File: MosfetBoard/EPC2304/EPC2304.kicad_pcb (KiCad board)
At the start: 4 copper layers, 120 x 75 mm, 176 parts, among them J10 DriverConn, J14 BATT-Conn2, J4 PhaseConn, J5 PhaseConn, J6 PhaseConn, J7 DriverConn, J8 DriverConn, J9 BATT-Conn1, Q1 EPC2304, Q13 EPC2304, Q14 EPC2304, Q15 EPC2304, Q2 EPC2304, Q3 EPC2304, Q4 EPC2304, Q5 EPC2304, Q6 EPC2304, Q7 EPC2304, Q8 EPC2304, Q9 EPC2304, U1 2EDF7275KXUMA1, U2 2EDF7275KXUMA1, U3 2EDF7275KXUMA1, U4 MT9223CT-50BR5, U5 MT9223CT-50BR5, U6 MT9223CT-50BR5

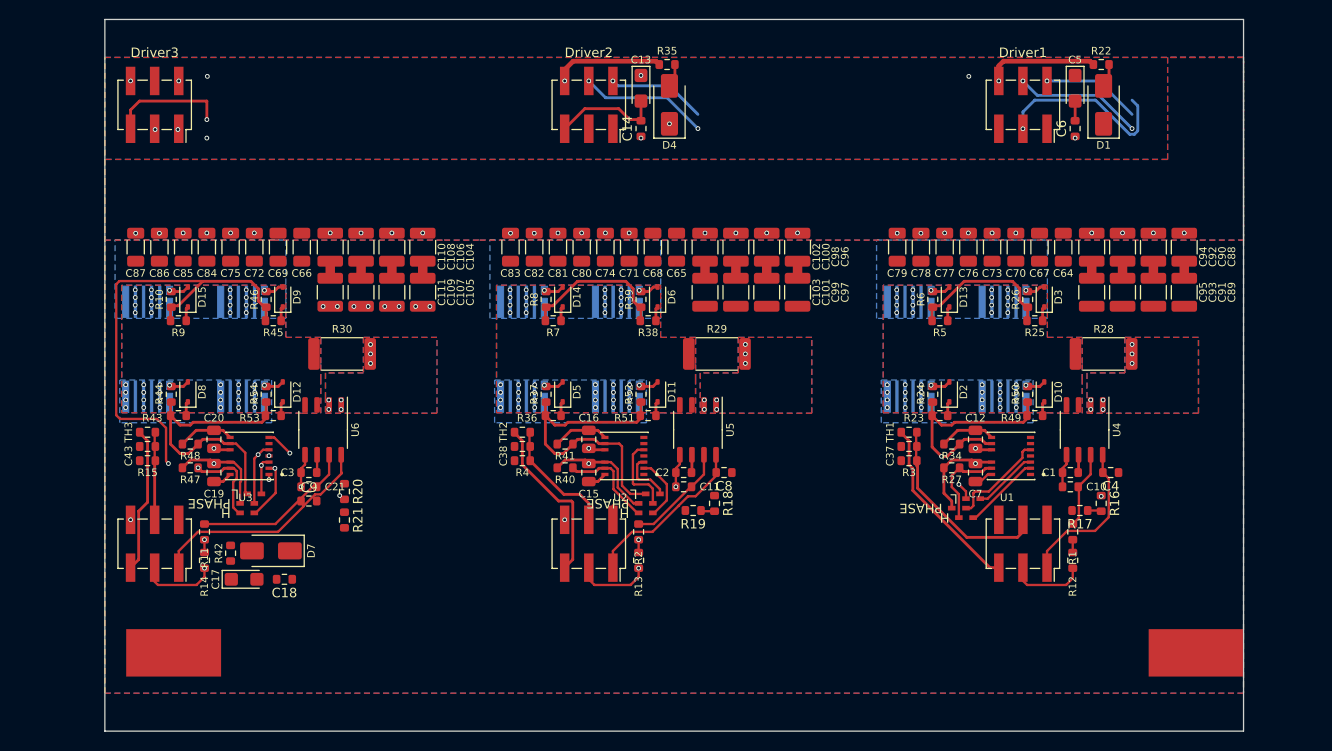
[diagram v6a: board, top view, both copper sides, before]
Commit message: v2.10.0 - Low side shunt and hall sensor - epc routed
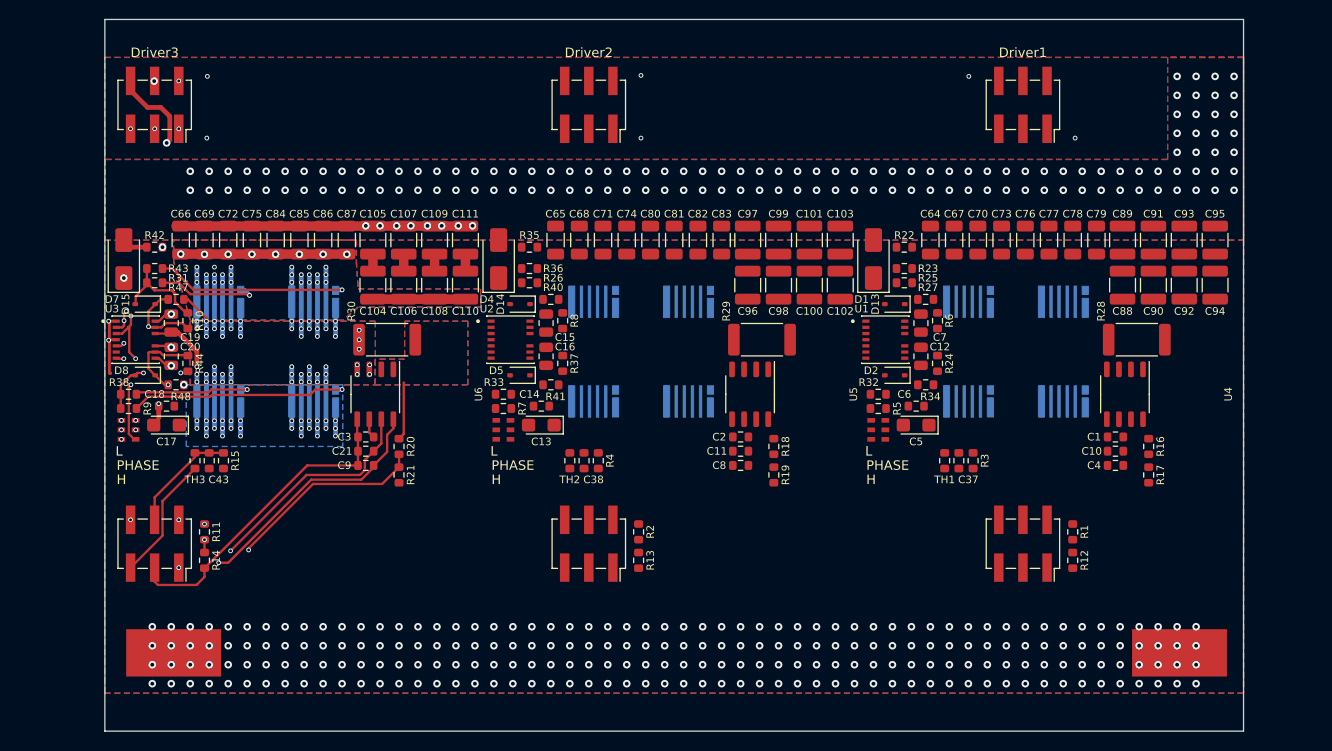
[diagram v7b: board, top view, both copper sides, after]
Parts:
- removed D10, D11, D12, D3, D6, D9: 1N5819WS, Diode_SMD:D_SOD-323
- removed R39, R46, R50, R52, R54: 10, Resistor_SMD:R_0603_1608Metric
- removed R45, R49, R51, R53: 1, Resistor_SMD:R_0603_1608Metric
- added R31: 2.2, Resistor_SMD:R_0603_1608Metric, F.Cu at (110.2, 81.8)
- added R32: 2.2, Resistor_SMD:R_0603_1608Metric, F.Cu at (186.5, 93.5)
- added R33: 2.2, Resistor_SMD:R_0603_1608Metric, F.Cu at (147.0, 93.5)
- R10, R24, R37, R44, R6, R8: value 10 -> 3.3
- R23, R25, R36, R38, R43, R5, R7, R9: value 1 -> 2.2
- R26: value 10 -> 2.2
- moved R38 55.3 mm to (107.5, 93.5)
- moved R26 52.5 mm to (149.8, 81.8), turned to 0 degrees
- moved C5 39.3 mm to (190.5, 96.8), turned to 180 degrees
- moved C13 37.0 mm to (151.0, 96.8), turned to 180 degrees
- moved D7 34.4 mm to (107.0, 79.2), turned to 90 degrees
- moved C6 33.7 mm to (190.5, 94.8), turned to 180 degrees
- moved R42 33.2 mm to (110.2, 78.0), turned to 180 degrees
- moved C14 31.1 mm to (151.0, 94.8), turned to 180 degrees
- moved D1 29.2 mm to (186.0, 79.2)
- moved R22 28.3 mm to (189.2, 78.0), turned to 180 degrees
- moved D4 24.2 mm to (146.5, 79.2)
- moved R35 24.1 mm to (149.8, 78.0), turned to 180 degrees
- moved C83 22.3 mm to (170.0, 77.2), turned to 90 degrees
- moved C87 22.3 mm to (130.5, 77.2), turned to 90 degrees
- moved C18 22.1 mm to (111.5, 94.8)
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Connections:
- D13 pad 1: Net-(D13-K) -> /PhaseMosfets1/PH
- D13 pad 2: Net-(D13-A) -> /PhaseMosfets1/HIGH
- D14 pad 1: Net-(D14-K) -> /PhaseMosfets2/PH
- D14 pad 2: Net-(D14-A) -> /PhaseMosfets2/HIGH
- D15 pad 1: Net-(D15-K) -> /PhaseMosfets3/PH
- D15 pad 2: Net-(D15-A) -> /PhaseMosfets3/HIGH
- D2 pad 1: Net-(D2-K) -> /PhaseMosfets1/PL
- D2 pad 2: Net-(D2-A) -> /PhaseMosfets1/LOW
- D5 pad 1: Net-(D5-K) -> /PhaseMosfets2/PL
- D5 pad 2: Net-(D5-A) -> /PhaseMosfets2/LOW
- D8 pad 1: Net-(D8-K) -> /PhaseMosfets3/PL
- D8 pad 2: Net-(D8-A) -> /PhaseMosfets3/LOW
- Q1 pad 1: Net-(D13-A) -> Net-(Q1-G)
- Q13 pad 1: Net-(D3-A) -> Net-(Q13-G)
- Q14 pad 1: Net-(D6-A) -> Net-(Q14-G)
- Q15 pad 1: Net-(D9-A) -> Net-(Q15-G)
- Q2 pad 1: Net-(D14-A) -> Net-(Q2-G)
- Q3 pad 1: Net-(D15-A) -> Net-(Q3-G)
- Q4 pad 1: Net-(D2-A) -> Net-(Q4-G)
- Q5 pad 1: Net-(D5-A) -> Net-(Q5-G)
- Q6 pad 1: Net-(D8-A) -> Net-(Q6-G)
- Q7 pad 1: Net-(D10-A) -> Net-(Q7-G)
- Q8 pad 1: Net-(D11-A) -> Net-(Q8-G)
- Q9 pad 1: Net-(D12-A) -> Net-(Q9-G)
- R10 pad 2: Net-(D15-A) -> /PhaseMosfets3/HIGH
- R23 pad 1: /PhaseMosfets1/PL -> /PhaseMosfets1/HIGH
- R23 pad 2: Net-(D2-K) -> Net-(Q13-G)
- R24 pad 2: Net-(D2-A) -> /PhaseMosfets1/LOW
- R25 pad 1: /PhaseMosfets1/PH -> /PhaseMosfets1/HIGH
- R25 pad 2: Net-(D3-K) -> Net-(Q1-G)
- R26 pad 1: /PhaseMosfets1/PH -> /PhaseMosfets2/HIGH
- R26 pad 2: Net-(D3-A) -> Net-(Q2-G)
- R36 pad 1: /PhaseMosfets2/PL -> /PhaseMosfets2/HIGH
- R36 pad 2: Net-(D5-K) -> Net-(Q14-G)
- R37 pad 2: Net-(D5-A) -> /PhaseMosfets2/LOW
- R38 pad 1: /PhaseMosfets2/PH -> /PhaseMosfets3/LOW
- R38 pad 2: Net-(D6-K) -> Net-(Q6-G)
- R43 pad 1: /PhaseMosfets3/PL -> /PhaseMosfets3/HIGH
- R43 pad 2: Net-(D8-K) -> Net-(Q15-G)
- R44 pad 2: Net-(D8-A) -> /PhaseMosfets3/LOW
- R5 pad 1: /PhaseMosfets1/PH -> /PhaseMosfets1/LOW
- R5 pad 2: Net-(D13-K) -> Net-(Q7-G)
- R6 pad 2: Net-(D13-A) -> /PhaseMosfets1/HIGH
- R7 pad 1: /PhaseMosfets2/PH -> /PhaseMosfets2/LOW
- R7 pad 2: Net-(D14-K) -> Net-(Q8-G)
- R8 pad 2: Net-(D14-A) -> /PhaseMosfets2/HIGH
- R9 pad 1: /PhaseMosfets3/PH -> /PhaseMosfets3/LOW
- R9 pad 2: Net-(D15-K) -> Net-(Q9-G)
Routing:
- net /PhaseMosfets3/PHASE: track 16.9 -> 149.1 mm, vias 41 -> 64
- net +BATT: track 0.00 -> 101.2 mm, vias 30 -> 170
- net -BATT: track 45.5 -> 135.6 mm, vias 20 -> 269
- net /PhaseMosfets1/DRV_POWER: track 66.8 -> 0.00 mm, vias 2 -> 0
- net /PhaseMosfets2/DRV_POWER: track 64.3 -> 0.00 mm, vias 2 -> 0
- net /PhaseMosfets3/3.3V_IN: track 86.1 -> 38.3 mm, vias 2 -> 3
- net /PhaseMosfets3/L: track 82.2 -> 34.6 mm, vias 2 -> 4
- net /PhaseMosfets3/LOCKOUT: track 81.3 -> 36.5 mm, vias 2 -> 3
- net /PhaseMosfets3/H: track 86.1 -> 43.1 mm, vias 2 -> 4
- net /PhaseMosfets3/PH: track 61.2 -> 22.0 mm
- net /PhaseMosfets2/PL: track 33.3 -> 0.00 mm
- net /PhaseMosfets1/PL: track 30.4 -> 0.00 mm, vias 2 -> 0
- net /PhaseMosfets3/V_SENSE: track 0.00 -> 29.8 mm, vias 1 -> 2
- net /PhaseMosfets1/L: track 26.4 -> 0.00 mm, vias 1 -> 0
- net /PhaseMosfets2/PH: track 26.0 -> 0.00 mm
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- removed copper zone on B.Cu, net /PhaseMosfets1/PHASE
- removed copper zone on F.Cu, net /PhaseMosfets1/PHASE
- removed copper zone on In1.Cu, net /PhaseMosfets1/PHASE
- removed copper zone on In2.Cu, net /PhaseMosfets1/PHASE
- removed copper zone on B.Cu, net /PhaseMosfets1/PHASE_OUT
- removed copper zone on F.Cu, net /PhaseMosfets1/PHASE_OUT
- removed copper zone on In1.Cu, net /PhaseMosfets1/PHASE_OUT
- removed copper zone on In2.Cu, net /PhaseMosfets1/PHASE_OUT
- removed copper zone on B.Cu, net /PhaseMosfets2/PHASE
- removed copper zone on F.Cu, net /PhaseMosfets2/PHASE
- removed copper zone on In1.Cu, net /PhaseMosfets2/PHASE
- removed copper zone on In2.Cu, net /PhaseMosfets2/PHASE
- removed copper zone on B.Cu, net /PhaseMosfets2/PHASE_OUT
- removed copper zone on F.Cu, net /PhaseMosfets2/PHASE_OUT
- removed copper zone on In1.Cu, net /PhaseMosfets2/PHASE_OUT
- removed copper zone on In2.Cu, net /PhaseMosfets2/PHASE_OUT
- removed copper zone on In2.Cu, net /PhaseMosfets3/PHASE

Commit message: v2.10.0 - Low side shunt and hall sensor - epc finished
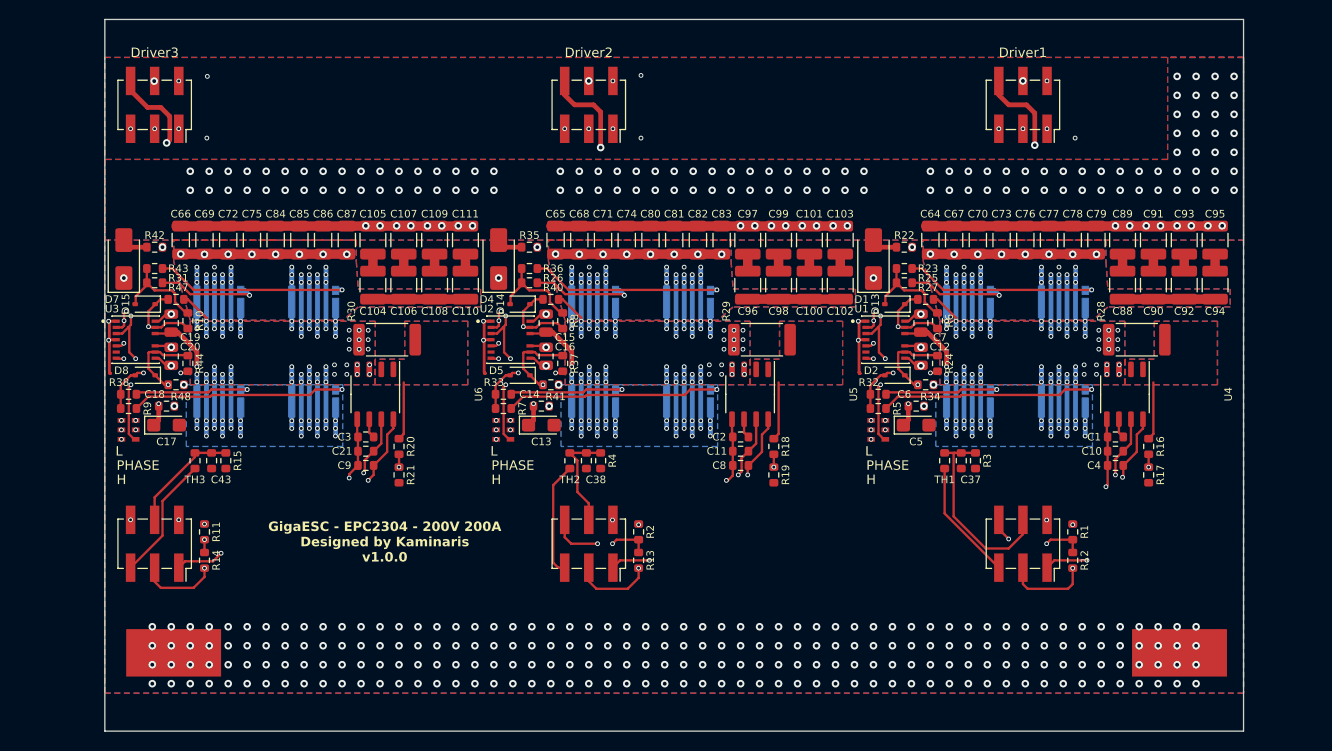
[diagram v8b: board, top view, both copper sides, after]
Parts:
- R10, R24, R37, R44, R6, R8: value 3.3 -> 4.7
- moved C37 0.25 mm to (195.2, 100.5)
- moved C38 0.25 mm to (155.8, 100.5)
- moved C43 0.25 mm to (116.2, 100.5)
- moved R15 0.25 mm to (117.8, 100.5)
- moved R3 0.25 mm to (196.8, 100.5)
- moved R4 0.25 mm to (157.2, 100.5)
- turned C13 to 0 degrees
- turned C17 to 0 degrees
- turned C5 to 0 degrees
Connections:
- C13 pad 1: -BATT -> /PhaseMosfets2/3.3V_IN
- C13 pad 2: /PhaseMosfets2/3.3V_IN -> -BATT
- C17 pad 1: -BATT -> /PhaseMosfets3/3.3V_IN
- C17 pad 2: /PhaseMosfets3/3.3V_IN -> -BATT
- C5 pad 1: -BATT -> /PhaseMosfets1/3.3V_IN
- C5 pad 2: /PhaseMosfets1/3.3V_IN -> -BATT
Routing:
- net -BATT: track 135.6 -> 416.3 mm, vias 269 -> 349
- net +BATT: track 101.2 -> 303.7 mm, vias 170 -> 236
- net /PhaseMosfets2/PHASE: track 0.00 -> 149.1 mm, vias 0 -> 74
- net /PhaseMosfets1/PHASE: track 0.00 -> 149.1 mm, vias 0 -> 74
- net /PhaseMosfets1/H: track 0.00 -> 53.0 mm, vias 0 -> 4
- net /PhaseMosfets1/3.3V_IN: track 0.00 -> 47.8 mm, vias 0 -> 3
- net /PhaseMosfets1/LOCKOUT: track 0.00 -> 47.3 mm, vias 0 -> 3
- net /PhaseMosfets2/H: track 0.00 -> 47.0 mm, vias 0 -> 4
- net /PhaseMosfets1/L: track 0.00 -> 44.7 mm, vias 0 -> 4
- net /PhaseMosfets1/DRV_POWER: track 0.00 -> 44.1 mm, vias 0 -> 3
- net /PhaseMosfets2/3.3V_IN: track 0.00 -> 41.5 mm, vias 0 -> 3
- net /PhaseMosfets2/LOCKOUT: track 0.00 -> 41.0 mm, vias 0 -> 3
- net /PhaseMosfets2/L: track 0.00 -> 38.4 mm, vias 0 -> 4
- net /PhaseMosfets2/DRV_POWER: track 0.00 -> 38.0 mm, vias 0 -> 3
- net /PhaseMosfets2/SH-: track 0.00 -> 31.8 mm, vias 0 -> 2
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- added copper zone on B.Cu, net /PhaseMosfets1/PHASE
- added copper zone on F.Cu, net /PhaseMosfets1/PHASE
- added copper zone on In1.Cu, net /PhaseMosfets1/PHASE
- added copper zone on B.Cu, net /PhaseMosfets1/PHASE_OUT
- added copper zone on F.Cu, net /PhaseMosfets1/PHASE_OUT
- added copper zone on In1.Cu, net /PhaseMosfets1/PHASE_OUT
- added copper zone on In2.Cu, net /PhaseMosfets1/PHASE_OUT
- added copper zone on B.Cu, net /PhaseMosfets2/PHASE
- added copper zone on F.Cu, net /PhaseMosfets2/PHASE
- added copper zone on In1.Cu, net /PhaseMosfets2/PHASE
- added copper zone on B.Cu, net /PhaseMosfets2/PHASE_OUT
- added copper zone on F.Cu, net /PhaseMosfets2/PHASE_OUT
- added copper zone on In1.Cu, net /PhaseMosfets2/PHASE_OUT
- added copper zone on In2.Cu, net /PhaseMosfets2/PHASE_OUT
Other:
- board text added: "Board Center X: 165 Y: 91.5"
- board text added: "GigaESC - EPC2304 - 200V 200A Designed by Kaminaris v1.0.0"
